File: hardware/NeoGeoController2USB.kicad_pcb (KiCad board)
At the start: 2 copper layers, 39.6 x 45.3 mm, 13 parts, among them CON1 AVR-ISP6, J1 USB, J2 DB15, U1 ATMEGA32U2-AU, X1 16Mhz

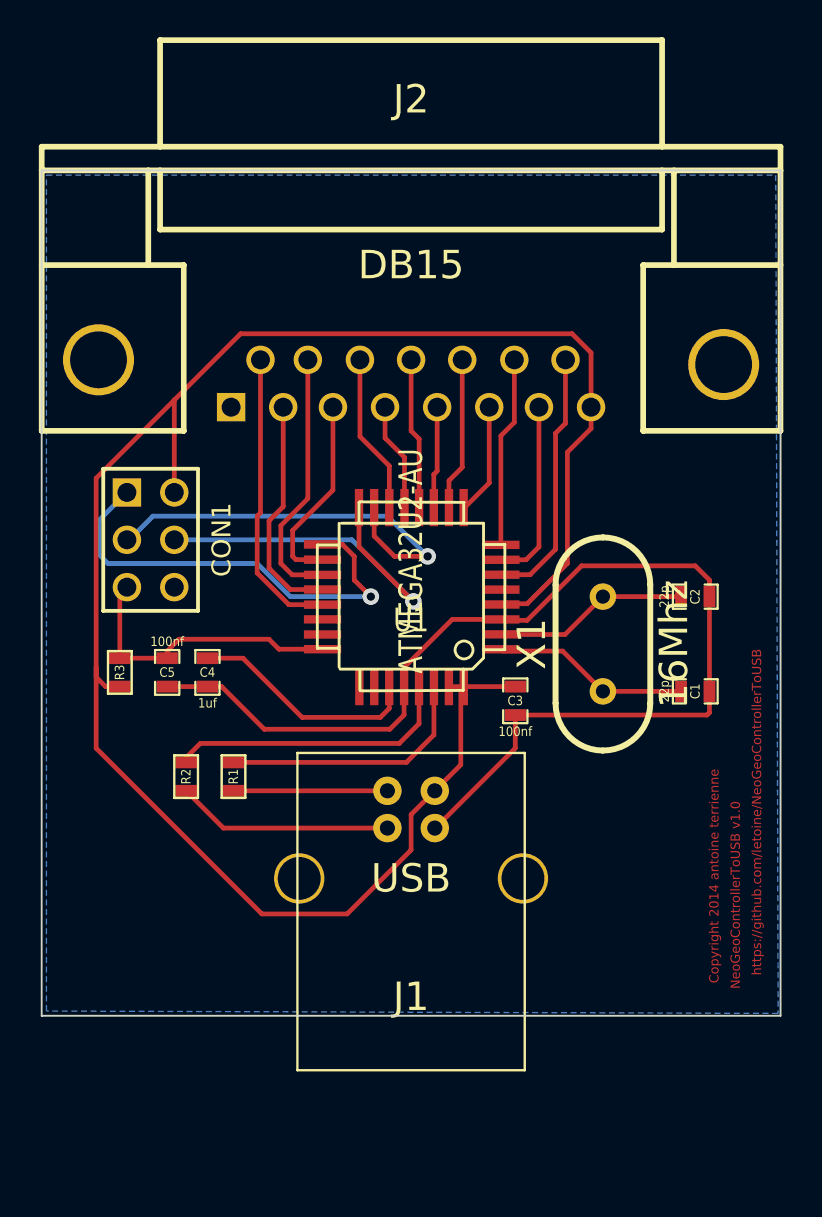
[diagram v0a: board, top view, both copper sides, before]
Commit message: Adding access to serial port. Fix controller pinout numering.
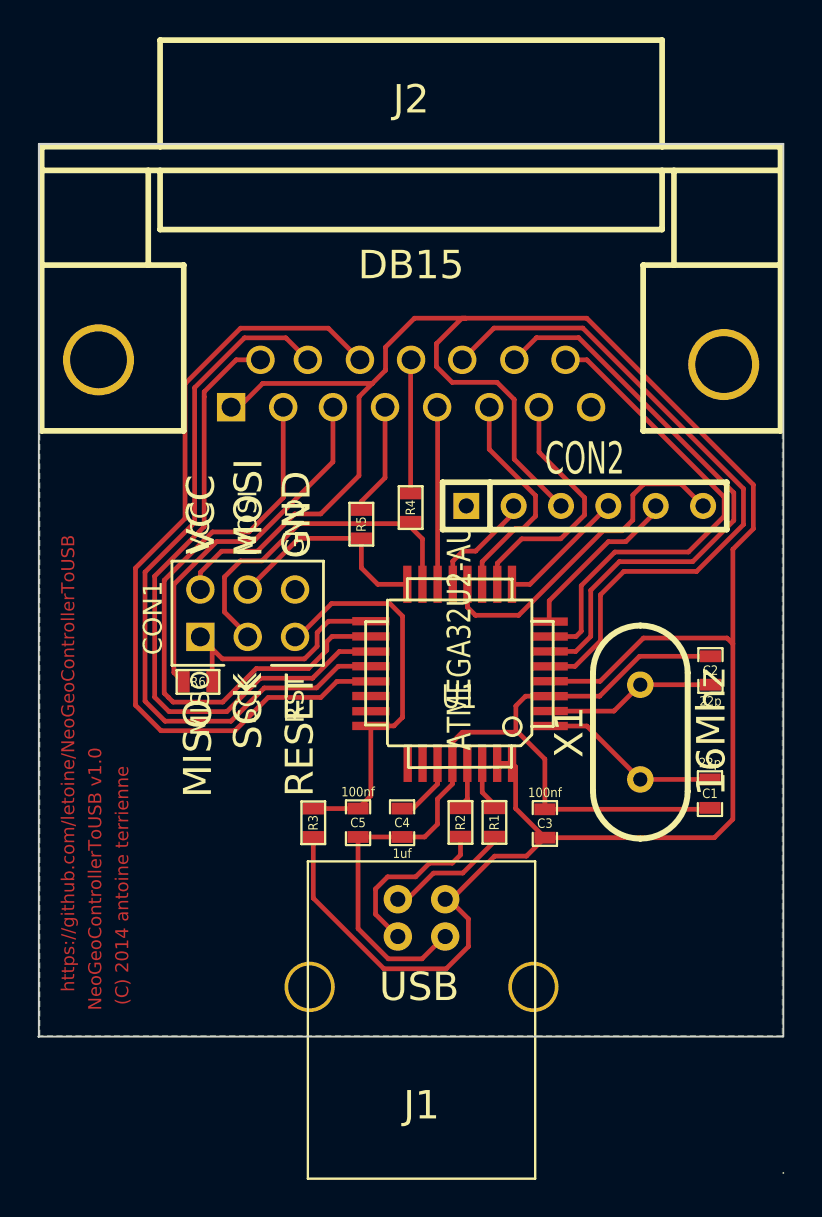
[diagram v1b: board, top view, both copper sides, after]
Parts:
- added CON2: TTL_6, SIL-6, F.Cu at (219.9, 138.6)
- added R4: 22ohms, SM0603, F.Cu at (210.5, 138.7)
- added R5: 22ohms, SM0603, F.Cu at (207.9, 139.6)
- added R6: 22ohms, SM0603, F.Cu at (199.1, 148.1)
- CON1: footprint pin_array_3x2 -> avr_isp_6
- moved R2 14.9 mm to (213.2, 155.6)
- moved R1 14.2 mm to (215.0, 155.6)
- moved C4 13.2 mm to (210.1, 155.6)
- moved R3 13.1 mm to (205.3, 155.6)
- moved C5 13.0 mm to (207.7, 155.6)
- moved C3 6.77 mm to (217.7, 155.7), turned to 270 degrees
- moved CON1 5.85 mm to (201.8, 143.1), turned to 90 degrees
- moved J1 5.84 mm to (211.1, 164.4)
- moved C1 5.54 mm to (226.6, 154.1), turned to 270 degrees
- moved X1 5.13 mm to (222.9, 150.8)
- moved U1 4.86 mm to (213.2, 147.6)
- moved C2 4.04 mm to (226.6, 147.5), turned to 90 degrees
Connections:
- J2 pad 1: GND -> VCC
- J2 pad 10: KICK_3 -> LEFT
- J2 pad 11: START -> A_BUTTON
- J2 pad 13: A_BUTTON -> START
- J2 pad 14: LEFT -> KICK_3
- J2 pad 15: UP -> D_KICK_2
- J2 pad 2: KICK_1 -> DOWN
- J2 pad 3: SELECT -> RIGHT
- J2 pad 4: D_BUTTON -> B_BUTTON
- J2 pad 5: B_BUTTON -> D_BUTTON
- J2 pad 6: RIGHT -> SELECT
- J2 pad 7: DOWN -> KICK_1
- J2 pad 8: VCC -> GND
- J2 pad 9: D_KICK_2 -> UP
- U1 pad 10: A_BUTTON -> KICK_1
- U1 pad 11: B_BUTTON -> SELECT
- U1 pad 12: C_BUTTON -> N-0000024
- U1 pad 13: D_BUTTON -> N-0000023
- U1 pad 14: START -> D_BUTTON
- U1 pad 18: SELECT -> DOWN
- U1 pad 19: KICK_3 -> UP
- U1 pad 20: KICK_1 -> LEFT
- U1 pad 21: D_KICK_2 -> A_BUTTON
- U1 pad 5: (no net) -> START
- U1 pad 6: UP -> KICK_3
- U1 pad 7: DOWN -> D_KICK_2
- U1 pad 8: LEFT -> N-0000025
- U1 pad 9: RIGHT -> N-0000022
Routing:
- net A_BUTTON: track 8.22 -> 43.9 mm
- net VCC: track 103.4 -> 135.1 mm
- net LEFT: track 10.2 -> 39.4 mm
- net START: track 8.58 -> 36.3 mm
- net DOWN: track 9.82 -> 32.1 mm
- net UP: track 13.9 -> 34.5 mm
- net N-0000024: track 0.00 -> 18.2 mm
- net KICK_3: track 14.0 -> 31.5 mm
- net RIGHT: track 5.98 -> 19.7 mm
- net N-0000032: track 15.5 -> 2.56 mm
- net N-0000011: track 13.9 -> 2.68 mm
- net GND: track 61.0 -> 50.3 mm
- net MISO: track 24.0 -> 13.6 mm, vias 1 -> 0
- net D_KICK_2: track 15.7 -> 26.1 mm
- net N-0000025: track 0.00 -> 9.12 mm
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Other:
- board size 39.6 x 45.3 mm -> 40 x 55.2 mm
- board text added: "(C) 2014 antoine terrienne"
- board text added: "GND"
- board text added: "MISO"
- board text added: "MOSI"
- board text added: "RESET"
- board text added: "SCK"
- board text added: "VCC"
- board text removed: "Copyright 2014 antoine terrienne"
